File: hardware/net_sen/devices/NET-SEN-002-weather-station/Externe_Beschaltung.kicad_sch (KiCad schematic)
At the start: 6 parts, among them SW1 SW_Push

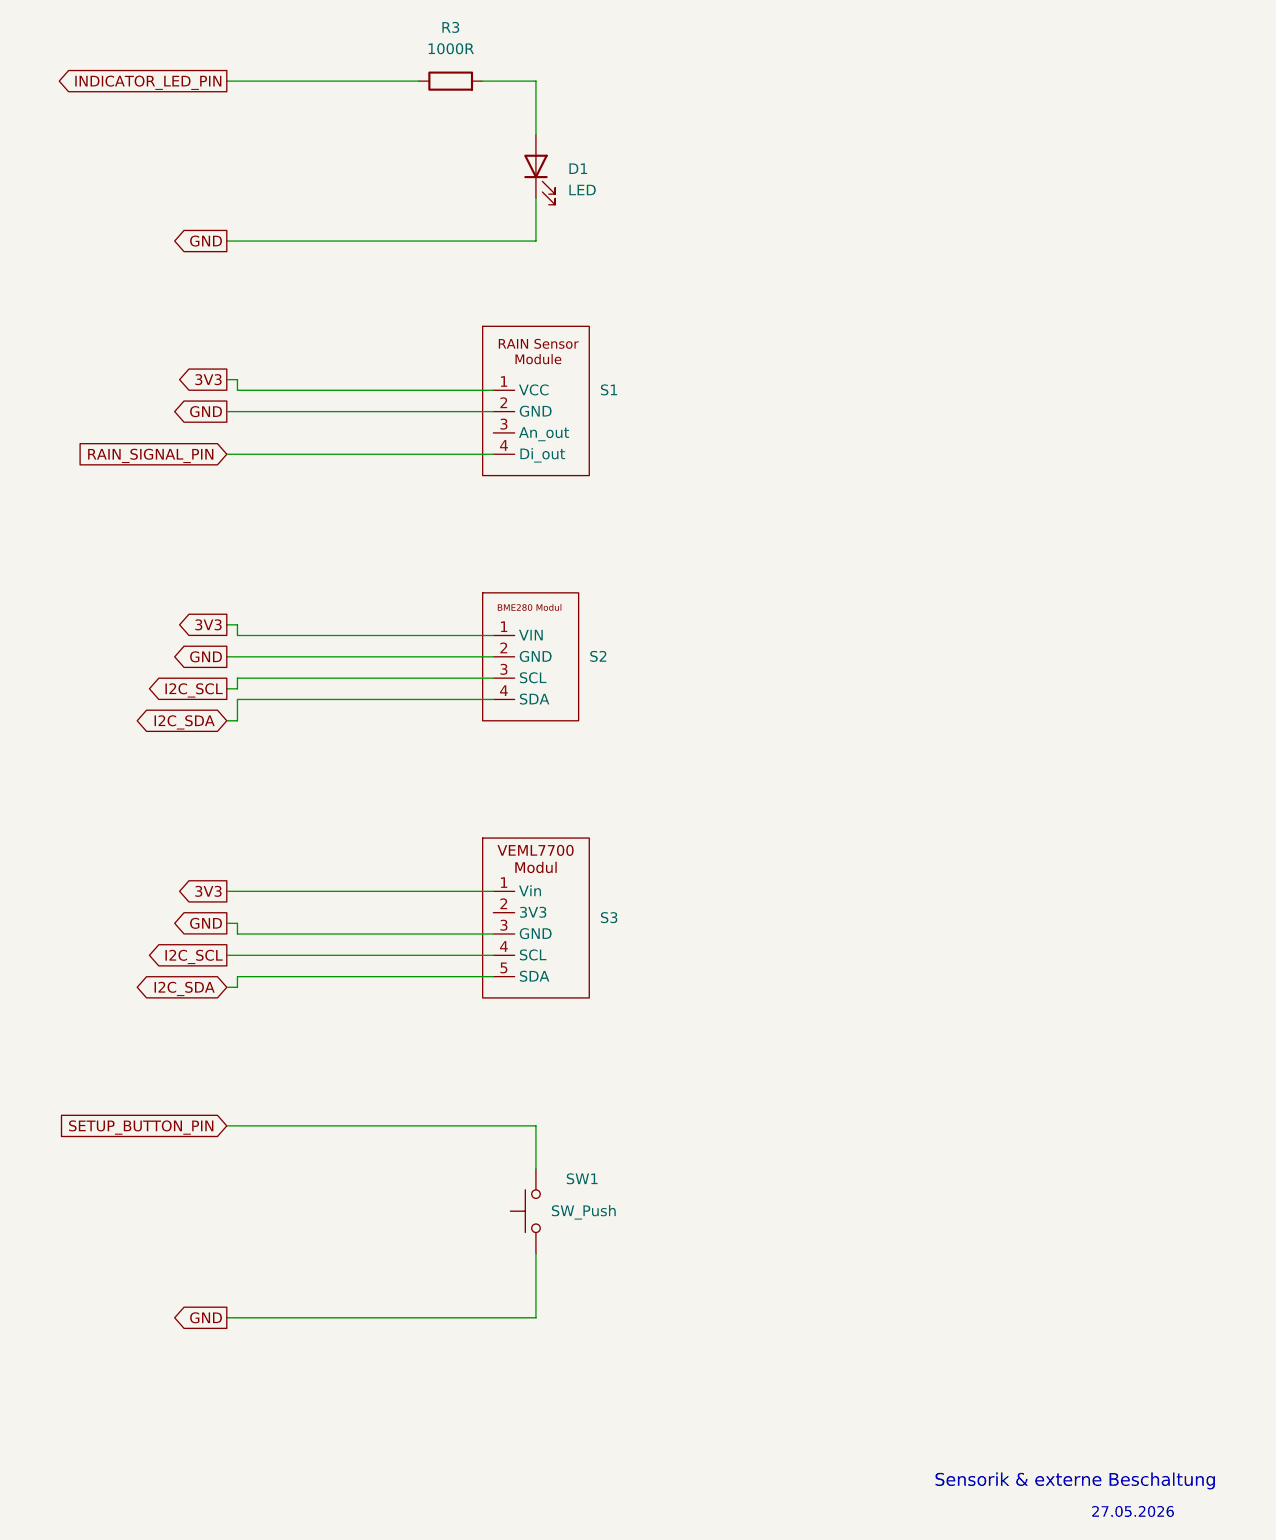
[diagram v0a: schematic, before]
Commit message: öffentliche Präsentation bereinigt: KI-Referenzen entfernt, READMEs optimiert, Firmware als Hauptlinie, ESPHome als Alternative mit Disclaimer
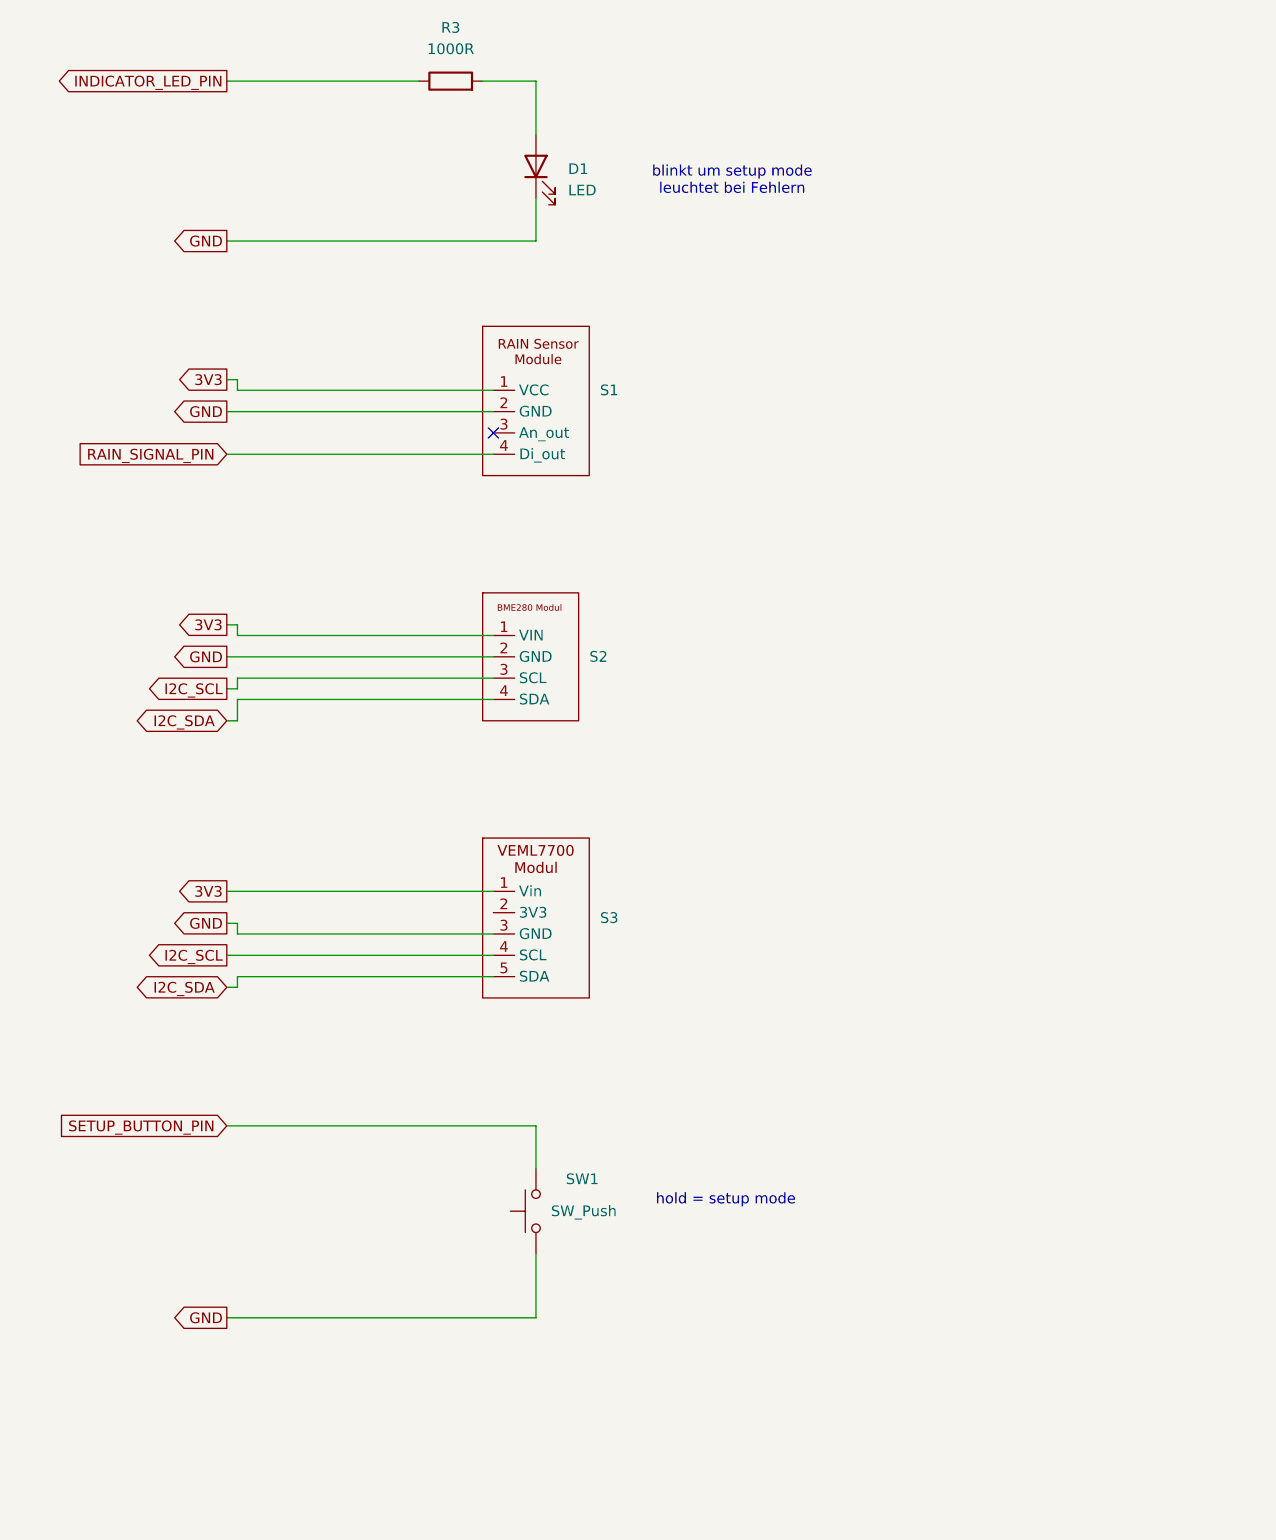
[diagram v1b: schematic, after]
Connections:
- no-connect marks 0 -> 1
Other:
- note added: "blinkt um setup mode leuchtet bei Fehlern"
- note added: "hold = setup mode"
- note removed: "27.05.2026"
- note removed: "Sensorik & externe Beschaltung"
- title: (none) -> Sensorik & externe Beschaltung
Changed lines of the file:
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@@
 	(generator_version "9.0")
 	(paper "A4")
-	(text "Sensorik & externe Beschaltung"
+	(title_block
+		(title "Sensorik & externe Beschaltung")
+		(date "2026-05-30")
+	)
+	(text "hold = setup mode"
 		(exclude_from_sim no)
-		(at 205.232 189.738 0)
-		(effects
-			(font
-				(size 1.524 1.524)
-			)
-		)
-	)
-	(text "27.05.2026"
+		(at 163.576 156.21 0)
+		(effects
+			(font
+				(size 1.27 1.27)
+			)
+		)
+	)
+	(text "blinkt um setup mode\nleuchtet bei Fehlern"
 		(exclude_from_sim no)
-		(at 212.09 193.548 0)
-		(effects
-			(font
-				(size 1.27 1.27)
-			)
-		)
+		(at 164.338 34.798 0)
+		(effects
+			(font
+				(size 1.27 1.27)
+			)
+		)
+	)
+	(no_connect
+		(at 135.89 64.77)
 	)
 	(wire
@@
 		(exclude_from_sim no)
 		(in_bom yes)
-		(on_board yes)
+		(on_board no)
 		(dnp no)
 		(fields_autoplaced yes)
@@
 		(exclude_from_sim no)
 		(in_bom yes)
-		(on_board yes)
+		(on_board no)
 		(dnp no)
 		(property "Reference" "SW1"
@@
 		(exclude_from_sim no)
 		(in_bom yes)
-		(on_board yes)
+		(on_board no)
 		(dnp no)
 		(fields_autoplaced yes)
